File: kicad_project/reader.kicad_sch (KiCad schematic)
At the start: 18 parts

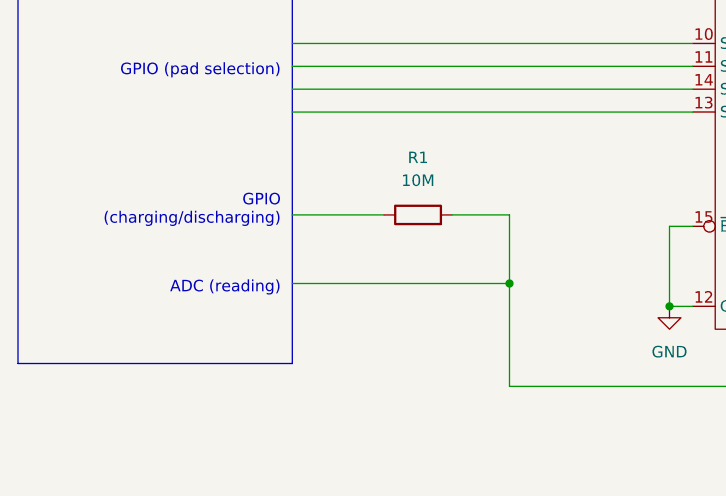
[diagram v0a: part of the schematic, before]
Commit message: Added Schmitt to schematic
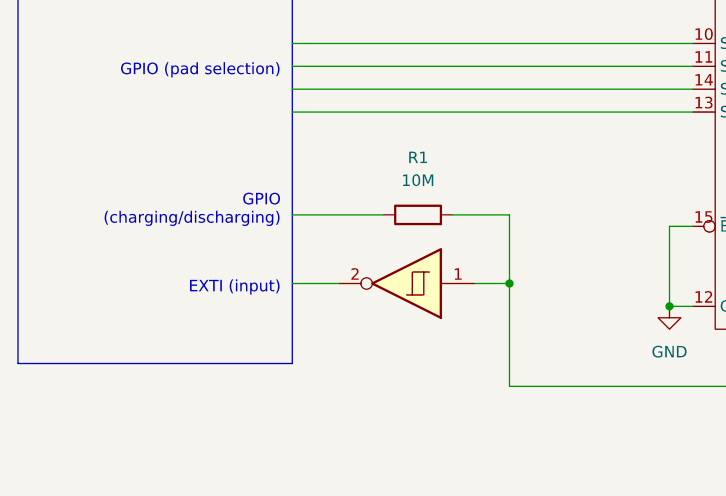
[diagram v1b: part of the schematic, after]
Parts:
- added U1: 74HC14, symbol 74xx:74HC14
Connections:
- net at MUX.1 (Z), R1.2: now also U1.1
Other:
- note added: "EXTI (input)"
- note removed: "ADC (reading)"
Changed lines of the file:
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@@
     (stroke (width 0) (type default))
   )
-  (wire (pts (xy 120.65 102.87) (xy 144.78 102.87))
+  (wire (pts (xy 120.65 102.87) (xy 125.73 102.87))
     (stroke (width 0) (type default))
   )
@@
     (stroke (width 0) (type default))
   )
+  (wire (pts (xy 140.97 102.87) (xy 144.78 102.87))
+    (stroke (width 0) (type default))
+  )
   (wire (pts (xy 199.39 100.33) (xy 199.39 90.17))
     (stroke (width 0) (type default))
@@
     (fill (type none))
   )
-  (text "ADC (reading)" (at 119.38 104.14 0)
+  (text "EXTI (input)" (at 119.38 104.14 0)
     (effects (font (size 1.27 1.27)) (justify right bottom))
   )
@@
         )
       )
+    )
+  )
+  (symbol (lib_id "74xx:74HC14") (at 133.35 102.87 180) (unit 1)
+    (in_bom yes) (on_board yes) (dnp no)
+    (property "Reference" "U1" (at 133.35 107.95 0)
+      (effects (font (size 1.27 1.27)) hide)
+    )
+    (property "Value" "74HC14" (at 133.35 110.49 0)
+      (effects (font (size 1.27 1.27)) hide)
+    )
+    (property "Footprint" "" (at 133.35 102.87 0)
+      (effects (font (size 1.27 1.27)) hide)
+    )
+    (property "Datasheet" "http://www.ti.com/lit/gpn/sn74HC14" (at 133.35 102.87 0)
+      (effects (font (size 1.27 1.27)) hide)
+    )
+    (pin "2")
+    (pin "1")
+    (pin "12")
+    (pin "4")
+    (pin "14")
+    (pin "7")
+    (pin "3")
+    (pin "13")
+    (pin "8")
+    (pin "5")
+    (pin "10")
+    (pin "11")
+    (pin "9")
+    (pin "6")
+    (instances
+      (project "gridcap"
+        (path "/78a49c71-2951-48b9-8f1e-813ada77e8b7/377411bc-5ddd-4767-b5f9-88461a75b2ce"
+          (reference "U1") (unit 1)
+        )
+      )

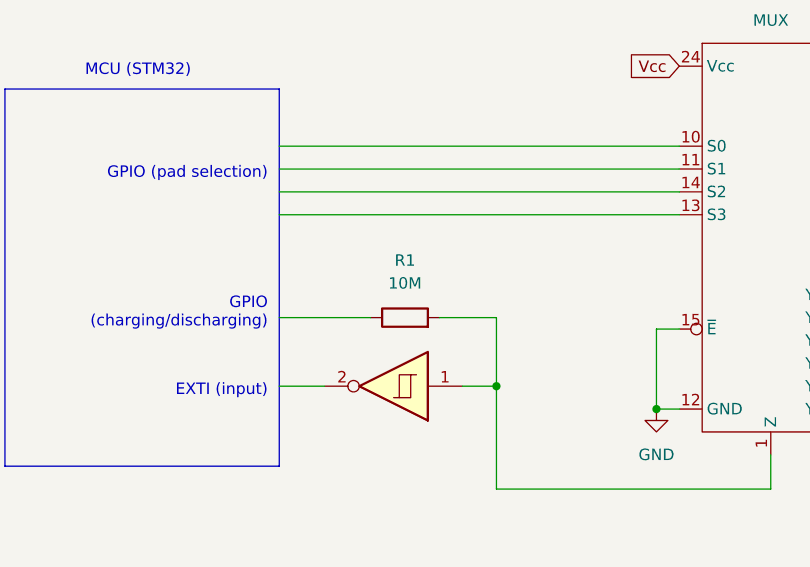
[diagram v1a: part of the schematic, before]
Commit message: Adjust resistance in schematic
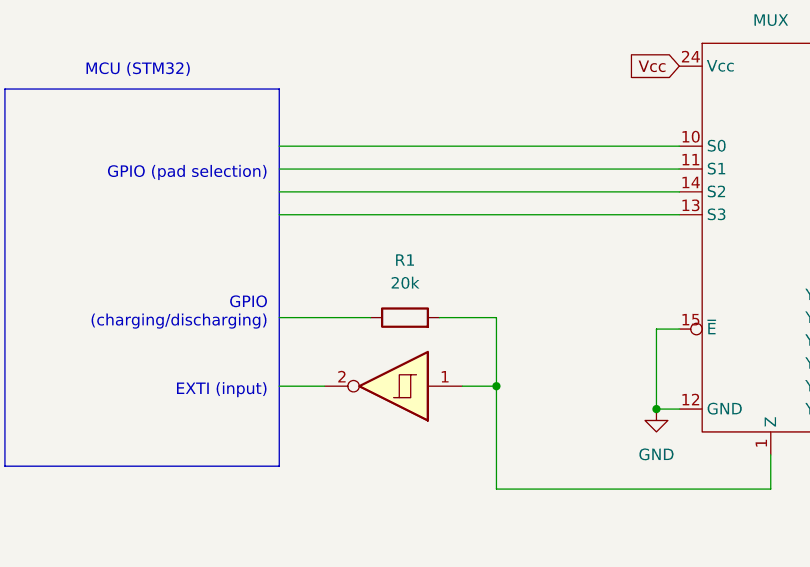
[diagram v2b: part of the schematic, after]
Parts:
- R1: value 10M -> 20k
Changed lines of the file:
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@@
       (effects (font (size 1.27 1.27)))
     )
-    (property "Value" "10M" (at 134.62 91.44 90)
+    (property "Value" "20k" (at 134.62 91.44 90)
       (effects (font (size 1.27 1.27)))
     )

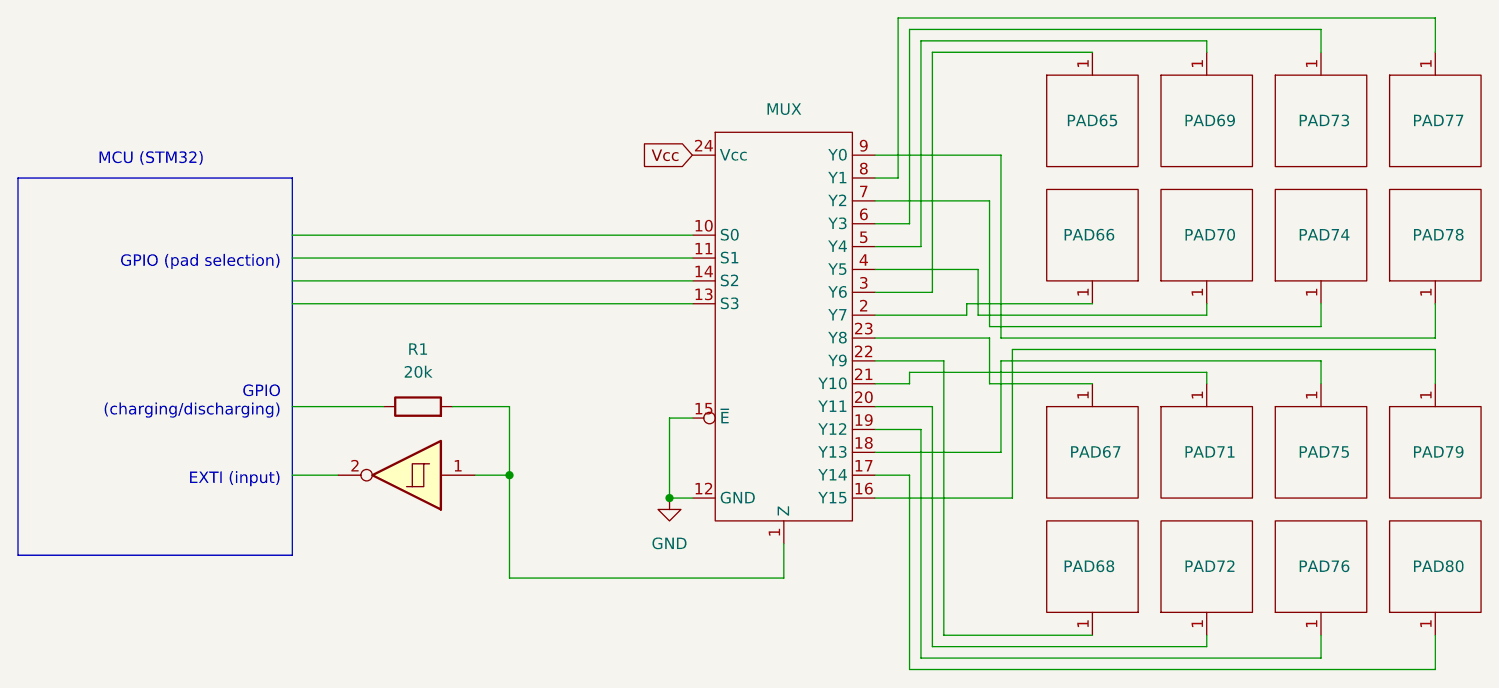
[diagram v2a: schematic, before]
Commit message: Update reading schematic to 220kohm
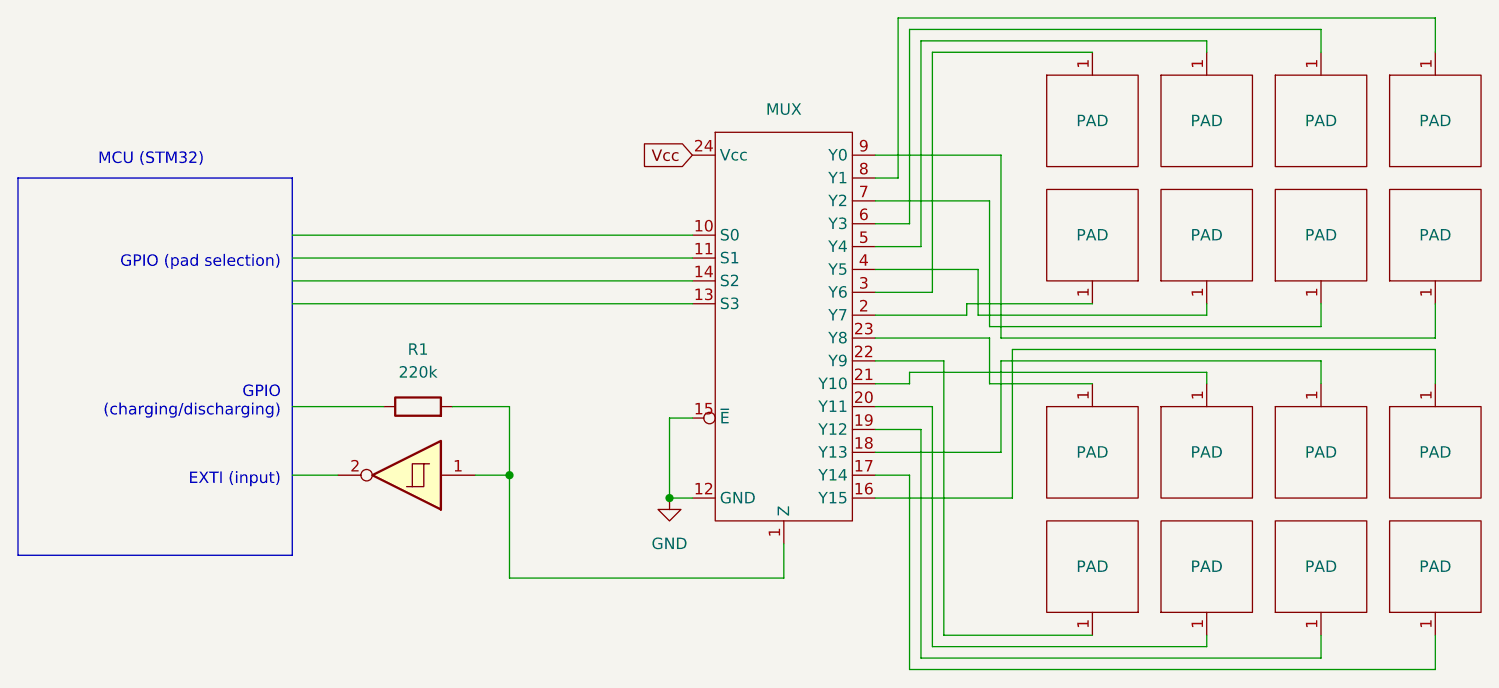
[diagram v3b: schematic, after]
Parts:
- R1: value 20k -> 220k
- renumbered PAD66 to PAD, PAD73 to PAD, PAD75 to PAD, PAD65 to PAD, PAD80 to PAD, PAD76 to PAD, PAD69 to PAD, PAD67 to PAD, PAD79 to PAD, PAD72 to PAD, PAD71 to PAD, PAD70 to PAD, PAD78 to PAD, PAD77 to PAD, PAD68 to PAD, PAD74 to PAD
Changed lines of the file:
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@@
   (symbol (lib_id "gridcap_symbols:CAPACITOR_PAD") (at 209.55 76.2 180) (unit 1)
     (in_bom yes) (on_board yes) (dnp no)
-    (property "Reference" "PAD66" (at 212.09 76.2 0)
-      (effects (font (size 1.27 1.27)) (justify left))
+    (property "Reference" "PAD" (at 209.55 76.2 0)
+      (effects (font (size 1.27 1.27)))
     )
     (property "Value" "~" (at 209.55 76.2 0)
@@
       (project "gridcap"
         (path "/78a49c71-2951-48b9-8f1e-813ada77e8b7/377411bc-5ddd-4767-b5f9-88461a75b2ce"
-          (reference "PAD66") (unit 1)
+          (reference "PAD") (unit 1)
         )
       )
@@
       (effects (font (size 1.27 1.27)))
     )
-    (property "Value" "20k" (at 134.62 91.44 90)
+    (property "Value" "220k" (at 134.62 91.44 90)
       (effects (font (size 1.27 1.27)))
     )
@@
   (symbol (lib_id "gridcap_symbols:CAPACITOR_PAD") (at 234.95 63.5 0) (unit 1)
     (in_bom yes) (on_board yes) (dnp no)
-    (property "Reference" "PAD73" (at 232.41 63.5 0)
-      (effects (font (size 1.27 1.27)) (justify left))
+    (property "Reference" "PAD" (at 234.95 63.5 0)
+      (effects (font (size 1.27 1.27)))
     )
     (property "Value" "~" (at 234.95 63.5 0)
@@
       (project "gridcap"
         (path "/78a49c71-2951-48b9-8f1e-813ada77e8b7/377411bc-5ddd-4767-b5f9-88461a75b2ce"
-          (reference "PAD73") (unit 1)
+          (reference "PAD") (unit 1)
         )
       )
@@
   (symbol (lib_id "gridcap_symbols:CAPACITOR_PAD") (at 234.95 100.33 0) (unit 1)
     (in_bom yes) (on_board yes) (dnp no)
-    (property "Reference" "PAD75" (at 232.41 100.33 0)
-      (effects (font (size 1.27 1.27)) (justify left))
+    (property "Reference" "PAD" (at 234.95 100.33 0)
+      (effects (font (size 1.27 1.27)))
     )
     (property "Value" "~" (at 234.95 100.33 0)
@@
       (project "gridcap"
         (path "/78a49c71-2951-48b9-8f1e-813ada77e8b7/377411bc-5ddd-4767-b5f9-88461a75b2ce"
-          (reference "PAD75") (unit 1)
+          (reference "PAD") (unit 1)
         )
       )
@@
   (symbol (lib_id "gridcap_symbols:CAPACITOR_PAD") (at 209.55 63.5 0) (unit 1)
     (in_bom yes) (on_board yes) (dnp no)
-    (property "Reference" "PAD65" (at 209.55 63.5 0)
+    (property "Reference" "PAD" (at 209.55 63.5 0)
       (effects (font (size 1.27 1.27)))
     )
@@
       (project "gridcap"
         (path "/78a49c71-2951-48b9-8f1e-813ada77e8b7/377411bc-5ddd-4767-b5f9-88461a75b2ce"
-          (reference "PAD65") (unit 1)
+          (reference "PAD") (unit 1)
         )
       )
@@
   (symbol (lib_id "gridcap_symbols:CAPACITOR_PAD") (at 247.65 113.03 0) (mirror x) (unit 1)
     (in_bom yes) (on_board yes) (dnp no)
-    (property "Reference" "PAD80" (at 245.11 113.03 0)
-      (effects (font (size 1.27 1.27)) (justify left))
+    (property "Reference" "PAD" (at 247.65 113.03 0)
+      (effects (font (size 1.27 1.27)))
     )
     (property "Value" "~" (at 247.65 113.03 0)
@@
       (project "gridcap"
         (path "/78a49c71-2951-48b9-8f1e-813ada77e8b7/377411bc-5ddd-4767-b5f9-88461a75b2ce"
-          (reference "PAD80") (unit 1)
+          (reference "PAD") (unit 1)
         )
       )
@@
   (symbol (lib_id "gridcap_symbols:CAPACITOR_PAD") (at 234.95 113.03 0) (mirror x) (unit 1)
     (in_bom yes) (on_board yes) (dnp no)
-    (property "Reference" "PAD76" (at 232.41 113.03 0)
-      (effects (font (size 1.27 1.27)) (justify left))
+    (property "Reference" "PAD" (at 234.95 113.03 0)
+      (effects (font (size 1.27 1.27)))
     )
     (property "Value" "~" (at 234.95 113.03 0)
@@
       (project "gridcap"
         (path "/78a49c71-2951-48b9-8f1e-813ada77e8b7/377411bc-5ddd-4767-b5f9-88461a75b2ce"
-          (reference "PAD76") (unit 1)
+          (reference "PAD") (unit 1)
         )
       )
@@
   (symbol (lib_id "gridcap_symbols:CAPACITOR_PAD") (at 222.25 63.5 0) (unit 1)
     (in_bom yes) (on_board yes) (dnp no)
-    (property "Reference" "PAD69" (at 219.71 63.5 0)
-      (effects (font (size 1.27 1.27)) (justify left))
+    (property "Reference" "PAD" (at 222.25 63.5 0)
+      (effects (font (size 1.27 1.27)))
     )
     (property "Value" "~" (at 222.25 63.5 0)
@@
       (project "gridcap"
         (path "/78a49c71-2951-48b9-8f1e-813ada77e8b7/377411bc-5ddd-4767-b5f9-88461a75b2ce"
-          (reference "PAD69") (unit 1)
+          (reference "PAD") (unit 1)
         )
       )
@@
   (symbol (lib_id "gridcap_symbols:CAPACITOR_PAD") (at 209.55 100.33 0) (unit 1)
     (in_bom yes) (on_board yes) (dnp no)
-    (property "Reference" "PAD67" (at 207.01 100.33 0)
-      (effects (font (size 1.27 1.27)) (justify left))
+    (property "Reference" "PAD" (at 209.55 100.33 0)
+      (effects (font (size 1.27 1.27)))
     )
     (property "Value" "~" (at 209.55 100.33 0)
@@
       (project "gridcap"
         (path "/78a49c71-2951-48b9-8f1e-813ada77e8b7/377411bc-5ddd-4767-b5f9-88461a75b2ce"
-          (reference "PAD67") (unit 1)
+          (reference "PAD") (unit 1)
         )
       )
@@
   (symbol (lib_id "gridcap_symbols:CAPACITOR_PAD") (at 247.65 100.33 0) (unit 1)
     (in_bom yes) (on_board yes) (dnp no)
-    (property "Reference" "PAD79" (at 245.11 100.33 0)
-      (effects (font (size 1.27 1.27)) (justify left))
+    (property "Reference" "PAD" (at 247.65 100.33 0)
+      (effects (font (size 1.27 1.27)))
     )
     (property "Value" "~" (at 247.65 100.33 0)
@@
       (project "gridcap"
         (path "/78a49c71-2951-48b9-8f1e-813ada77e8b7/377411bc-5ddd-4767-b5f9-88461a75b2ce"
-          (reference "PAD79") (unit 1)
+          (reference "PAD") (unit 1)
         )
       )
@@
   (symbol (lib_id "gridcap_symbols:CAPACITOR_PAD") (at 222.25 113.03 0) (mirror x) (unit 1)
     (in_bom yes) (on_board yes) (dnp no)
-    (property "Reference" "PAD72" (at 219.71 113.03 0)
-      (effects (font (size 1.27 1.27)) (justify left))
+    (property "Reference" "PAD" (at 222.25 113.03 0)
+      (effects (font (size 1.27 1.27)))
     )
     (property "Value" "~" (at 222.25 113.03 0)
@@
       (project "gridcap"
         (path "/78a49c71-2951-48b9-8f1e-813ada77e8b7/377411bc-5ddd-4767-b5f9-88461a75b2ce"
-          (reference "PAD72") (unit 1)
+          (reference "PAD") (unit 1)
         )
       )
@@
   (symbol (lib_id "gridcap_symbols:CAPACITOR_PAD") (at 222.25 100.33 0) (unit 1)
     (in_bom yes) (on_board yes) (dnp no)
-    (property "Reference" "PAD71" (at 219.71 100.33 0)
-      (effects (font (size 1.27 1.27)) (justify left))
+    (property "Reference" "PAD" (at 222.25 100.33 0)
+      (effects (font (size 1.27 1.27)))
     )
     (property "Value" "~" (at 222.25 100.33 0)
@@
       (project "gridcap"
         (path "/78a49c71-2951-48b9-8f1e-813ada77e8b7/377411bc-5ddd-4767-b5f9-88461a75b2ce"
-          (reference "PAD71") (unit 1)
+          (reference "PAD") (unit 1)
         )
       )
@@
   (symbol (lib_id "gridcap_symbols:CAPACITOR_PAD") (at 222.25 76.2 0) (mirror x) (unit 1)
     (in_bom yes) (on_board yes) (dnp no)
-    (property "Reference" "PAD70" (at 219.71 76.2 0)
-      (effects (font (size 1.27 1.27)) (justify left))
+    (property "Reference" "PAD" (at 222.25 76.2 0)
+      (effects (font (size 1.27 1.27)))
     )
     (property "Value" "~" (at 222.25 76.2 0)
@@
       (project "gridcap"
         (path "/78a49c71-2951-48b9-8f1e-813ada77e8b7/377411bc-5ddd-4767-b5f9-88461a75b2ce"
-          (reference "PAD70") (unit 1)
+          (reference "PAD") (unit 1)
         )
       )
@@
   (symbol (lib_id "gridcap_symbols:CAPACITOR_PAD") (at 247.65 76.2 0) (mirror x) (unit 1)
     (in_bom yes) (on_board yes) (dnp no)
-    (property "Reference" "PAD78" (at 245.11 76.2 0)
-      (effects (font (size 1.27 1.27)) (justify left))
+    (property "Reference" "PAD" (at 247.65 76.2 0)
+      (effects (font (size 1.27 1.27)))
     )
     (property "Value" "~" (at 247.65 76.2 0)
@@
       (project "gridcap"
         (path "/78a49c71-2951-48b9-8f1e-813ada77e8b7/377411bc-5ddd-4767-b5f9-88461a75b2ce"
-          (reference "PAD78") (unit 1)
+          (reference "PAD") (unit 1)
         )
       )
@@
   (symbol (lib_id "gridcap_symbols:CAPACITOR_PAD") (at 247.65 63.5 0) (unit 1)
     (in_bom yes) (on_board yes) (dnp no)
-    (property "Reference" "PAD77" (at 245.11 63.5 0)
-      (effects (font (size 1.27 1.27)) (justify left))
+    (property "Reference" "PAD" (at 247.65 63.5 0)
+      (effects (font (size 1.27 1.27)))
     )
     (property "Value" "~" (at 247.65 63.5 0)
@@
       (project "gridcap"
         (path "/78a49c71-2951-48b9-8f1e-813ada77e8b7/377411bc-5ddd-4767-b5f9-88461a75b2ce"
-          (reference "PAD77") (unit 1)
+          (reference "PAD") (unit 1)
         )
       )
@@
   (symbol (lib_id "gridcap_symbols:CAPACITOR_PAD") (at 209.55 113.03 180) (unit 1)
     (in_bom yes) (on_board yes) (dnp no)
-    (property "Reference" "PAD68" (at 212.09 113.03 0)
-      (effects (font (size 1.27 1.27)) (justify left))
+    (property "Reference" "PAD" (at 209.55 113.03 0)
+      (effects (font (size 1.27 1.27)))
     )
     (property "Value" "~" (at 209.55 113.03 0)
@@
       (project "gridcap"
         (path "/78a49c71-2951-48b9-8f1e-813ada77e8b7/377411bc-5ddd-4767-b5f9-88461a75b2ce"
-          (reference "PAD68") (unit 1)
+          (reference "PAD") (unit 1)
         )
       )
@@
   (symbol (lib_id "gridcap_symbols:CAPACITOR_PAD") (at 234.95 76.2 0) (mirror x) (unit 1)
     (in_bom yes) (on_board yes) (dnp no)
-    (property "Reference" "PAD74" (at 232.41 76.2 0)
-      (effects (font (size 1.27 1.27)) (justify left))
+    (property "Reference" "PAD" (at 234.95 76.2 0)
+      (effects (font (size 1.27 1.27)))
     )
     (property "Value" "~" (at 234.95 76.2 0)
@@
       (project "gridcap"
         (path "/78a49c71-2951-48b9-8f1e-813ada77e8b7/377411bc-5ddd-4767-b5f9-88461a75b2ce"
-          (reference "PAD74") (unit 1)
-        )
-      )
+          (reference "PAD") (unit 1)
+        )
+      )
